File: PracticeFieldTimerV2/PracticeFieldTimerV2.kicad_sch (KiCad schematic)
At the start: 17 parts, among them J1 External Controls, J3 Panel, J5 /CAN Enable, J6 RJ45, J7 RJ45, U1 ESP32-DevKitC

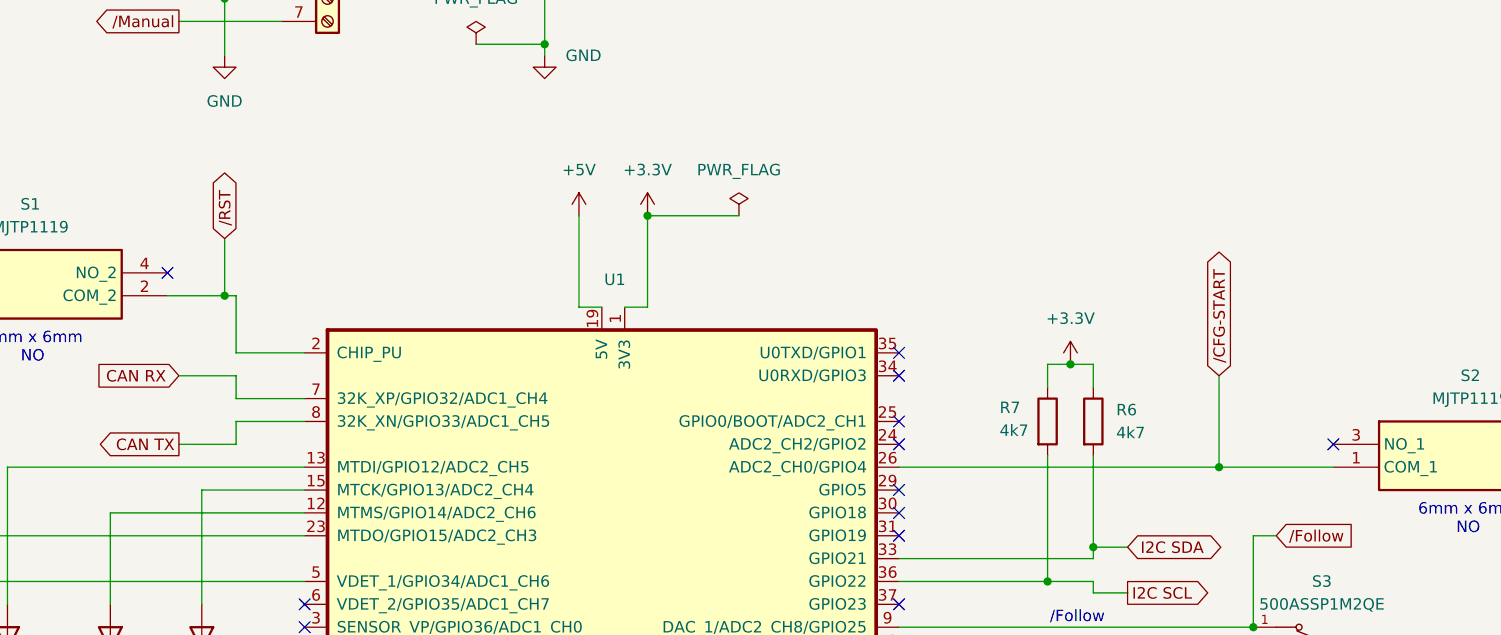
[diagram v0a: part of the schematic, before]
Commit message: Fix push button connections.
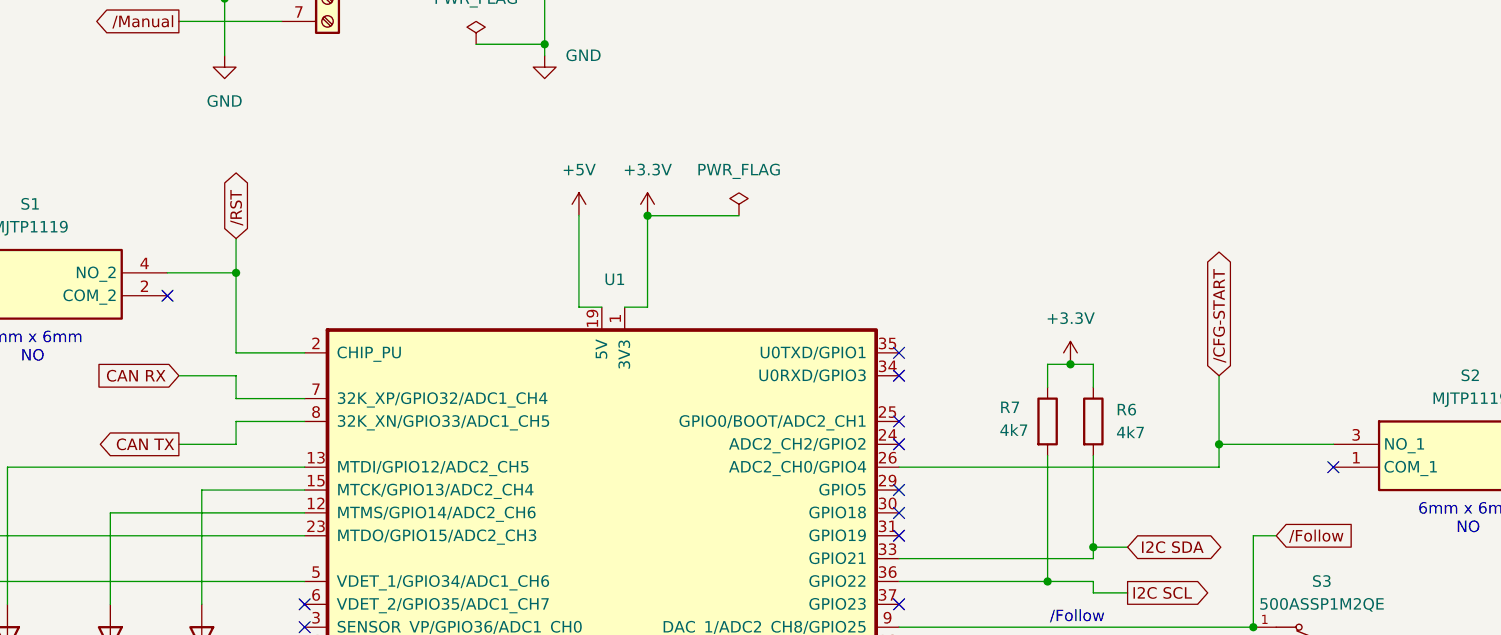
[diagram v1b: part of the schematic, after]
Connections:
- net /CFG-START: now also S2.3 (NO_1); no longer S2.1 (COM_1)
- net /RST: now also S1.4 (NO_2); no longer S1.2 (COM_2)
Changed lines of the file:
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@@
+	)
+	(junction
+		(at 204.47 85.09)
+		(diameter 0)
+		(color 0 0 0 0)
 	)
 	(junction
@@
 	)
 	(junction
-		(at 204.47 87.63)
-		(diameter 0)
-		(color 0 0 0 0)
-	)
-	(junction
 		(at 93.98 30.48)
 		(diameter 0)
@@
 	)
 	(junction
-		(at 93.98 68.58)
+		(at 95.25 66.04)
 		(diameter 0)
 		(color 0 0 0 0)
@@
 	)
 	(no_connect
-		(at 217.17 85.09)
+		(at 217.17 87.63)
 	)
 	(no_connect
@@
 	)
 	(no_connect
-		(at 87.63 66.04)
+		(at 87.63 68.58)
 	)
 	(no_connect
@@
 	(wire
 		(pts
+			(xy 204.47 85.09) (xy 204.47 87.63)
+		)
+		(stroke
+			(width 0)
+			(type default)
+		)
+	)
+	(wire
+		(pts
 			(xy 208.28 120.65) (xy 208.28 110.49)
 		)
@@
 	(wire
 		(pts
+			(xy 204.47 85.09) (xy 217.17 85.09)
+		)
+		(stroke
+			(width 0)
+			(type default)
+		)
+	)
+	(wire
+		(pts
 			(xy 121.92 40.64) (xy 129.54 40.64)
 		)
@@
 	(wire
 		(pts
-			(xy 204.47 87.63) (xy 217.17 87.63)
-		)
-		(stroke
-			(width 0)
-			(type default)
-		)
-	)
-	(wire
-		(pts
-			(xy 95.25 68.58) (xy 95.25 74.93)
-		)
-		(stroke
-			(width 0)
-			(type default)
-		)
-	)
-	(wire
-		(pts
 			(xy 135.89 179.07) (xy 135.89 181.61)
 		)
@@
 	(wire
 		(pts
+			(xy 87.63 66.04) (xy 95.25 66.04)
+		)
+		(stroke
+			(width 0)
+			(type default)
+		)
+	)
+	(wire
+		(pts
 			(xy 81.28 110.49) (xy 81.28 114.3)
 		)
@@
 	(wire
 		(pts
-			(xy 93.98 68.58) (xy 95.25 68.58)
+			(xy 95.25 66.04) (xy 95.25 74.93)
 		)
 		(stroke
@@
 	(wire
 		(pts
-			(xy 93.98 62.23) (xy 93.98 68.58)
+			(xy 95.25 62.23) (xy 95.25 66.04)
 		)
 		(stroke
@@
 	(wire
 		(pts
-			(xy 204.47 77.47) (xy 204.47 87.63)
+			(xy 204.47 77.47) (xy 204.47 85.09)
 		)
 		(stroke
@@
 		(pts
 			(xy 88.9 38.1) (xy 100.33 38.1)
-		)
-		(stroke
-			(width 0)
-			(type default)
-		)
-	)
-	(wire
-		(pts
-			(xy 87.63 68.58) (xy 93.98 68.58)
 		)
 		(stroke
@@
 	(global_label "{slash}RST"
 		(shape bidirectional)
-		(at 93.98 62.23 90)
+		(at 95.25 62.23 90)
 		(fields_autoplaced yes)
 		(effects
@@
 		)
 		(property "Intersheetrefs" "${INTERSHEET_REFS}"
-			(at 93.98 53.3559 90)
+			(at 95.25 53.3559 90)
 			(effects
 				(font

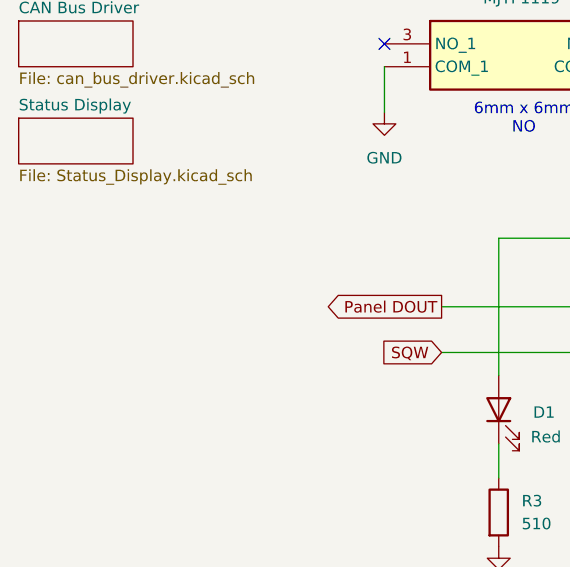
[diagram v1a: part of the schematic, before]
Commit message: Add DS3231
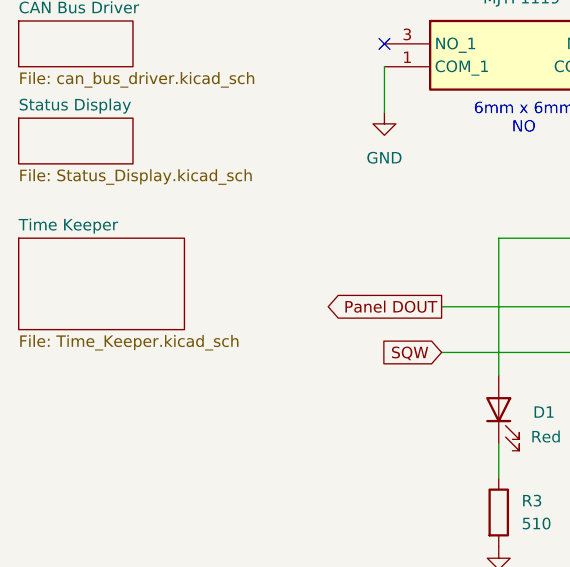
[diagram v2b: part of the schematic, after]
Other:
- added sheet Time Keeper (Time_Keeper.kicad_sch)
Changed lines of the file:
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@@
+	)
+	(sheet
+		(at 16.51 87.63)
+		(size 18.415 10.16)
+		(exclude_from_sim no)
+		(in_bom yes)
+		(on_board yes)
+		(dnp no)
+		(fields_autoplaced yes)
+		(stroke
+			(width 0.1524)
+			(type solid)
+		)
+		(fill
+			(color 0 0 0 0.0000)
+		)
+		(property "Sheetname" "Time Keeper"
+			(at 16.51 86.9184 0)
+			(effects
+				(font
+					(size 1.27 1.27)
+				)
+				(justify left bottom)
+			)
+		)
+		(property "Sheetfile" "Time_Keeper.kicad_sch"
+			(at 16.51 98.3746 0)
+			(effects
+				(font
+					(size 1.27 1.27)
+				)
+				(justify left top)
+			)
+		)
+		(instances
+			(project "PracticeFieldTimerV2"
+				(path "/a82ebad5-0442-461b-8944-6652da9a0796"
+					(page "4")
+				)
+			)
+		)
 	)
 	(sheet

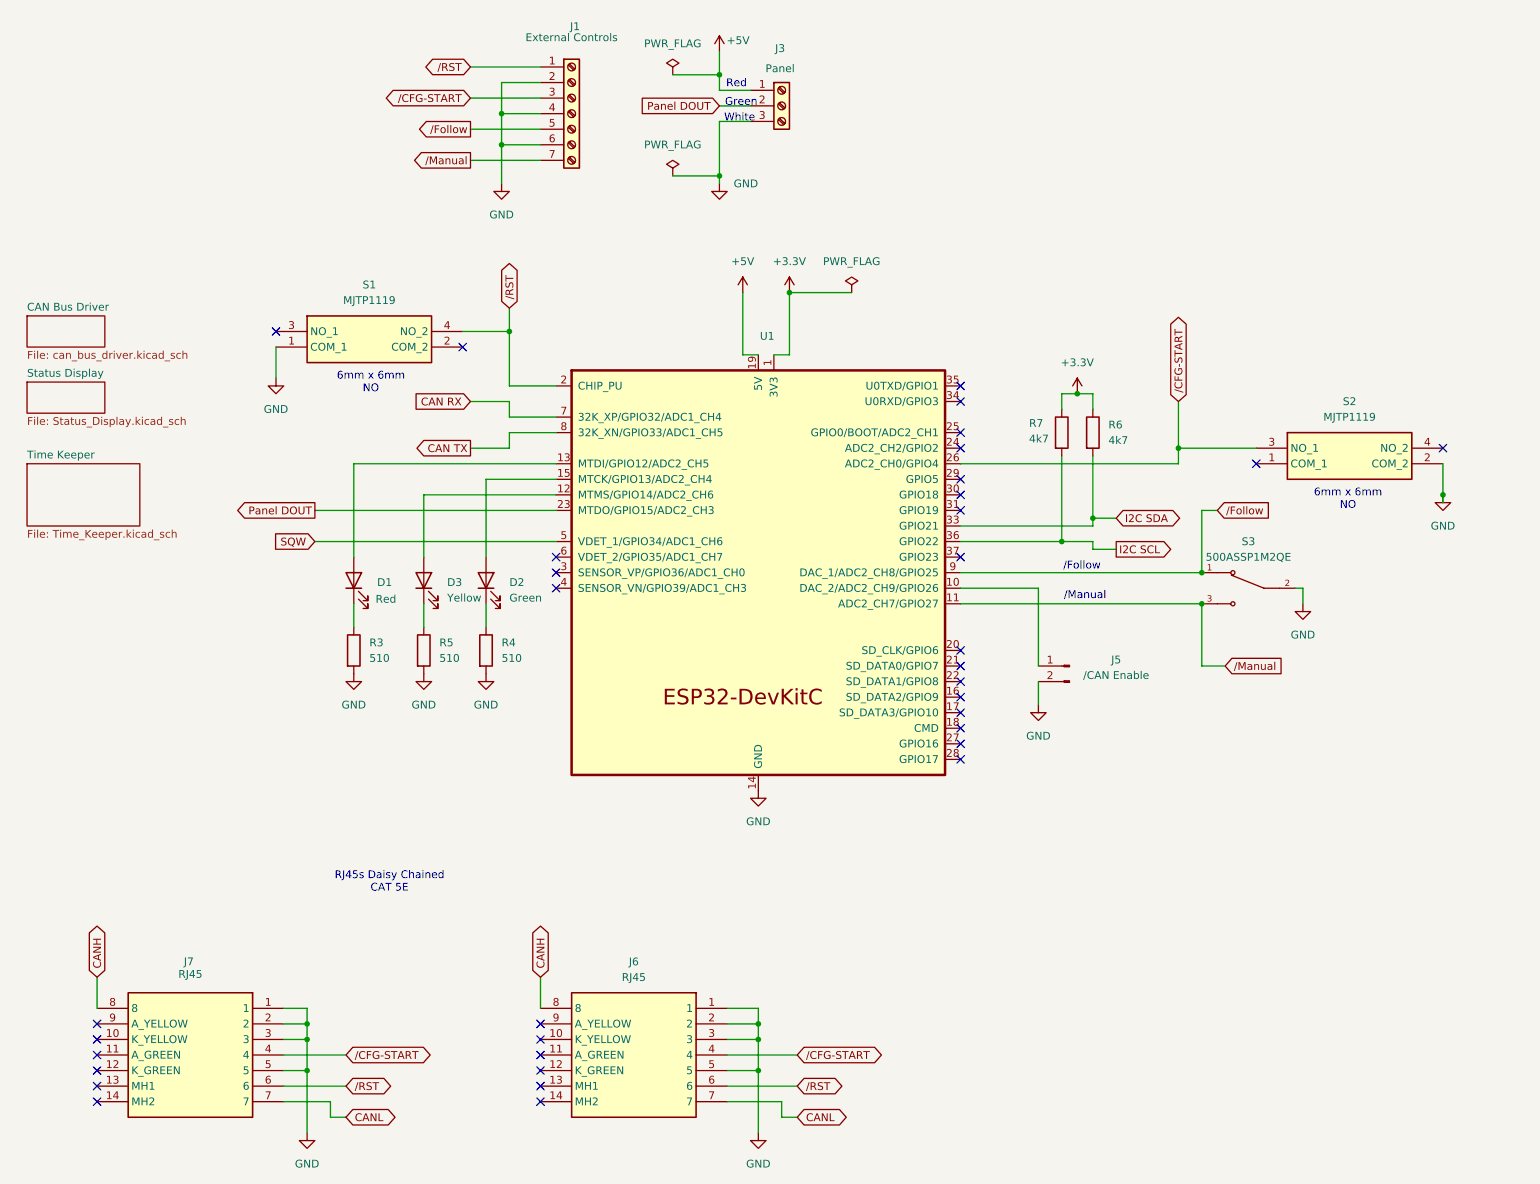
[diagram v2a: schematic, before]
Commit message: Morar blinkinlights: connect the LEDs on the RJ45 jacks to ESP32 pins. Can have too many blinkers!
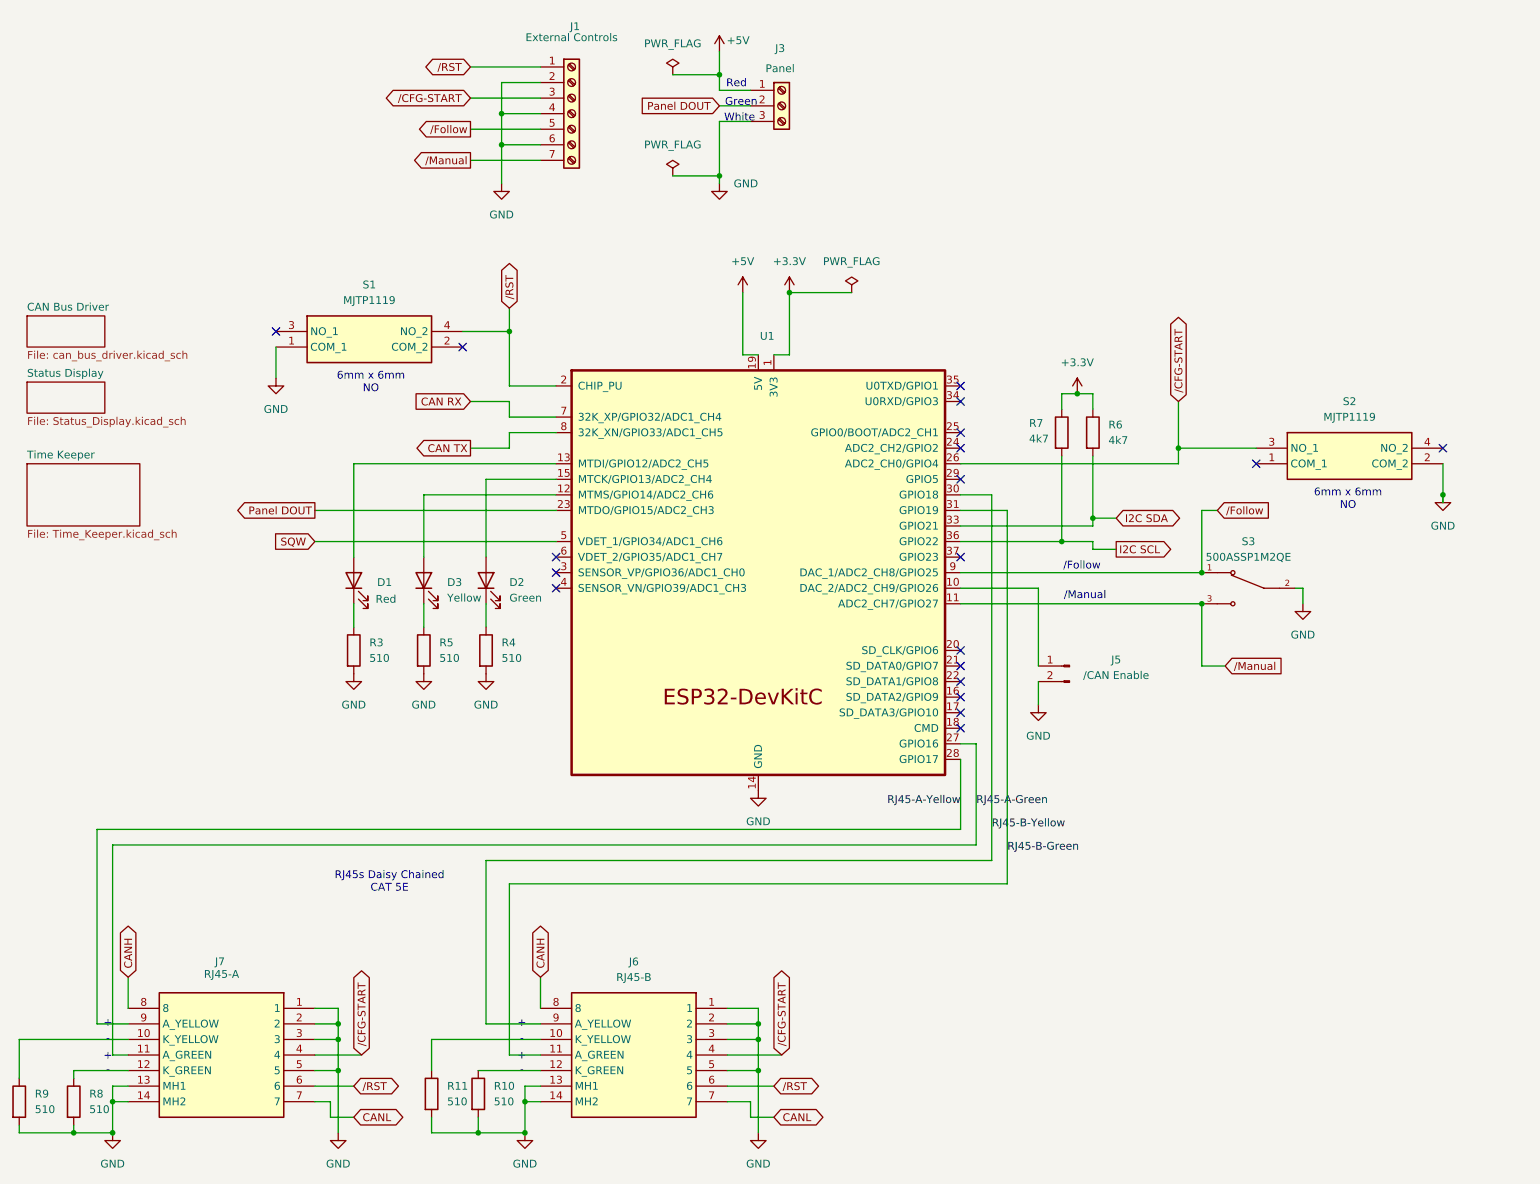
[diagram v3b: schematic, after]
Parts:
- added R10, R11, R8, R9: 510, Resistor_THT:R_Axial_DIN0207_L6.3mm_D2.5mm_P15.24mm_Horizontal, symbol Device:R
- J6: value RJ45 -> RJ45-B
- J7: value RJ45 -> RJ45-A
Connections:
- net GND: now also J6.13 (MH1), J6.14 (MH2), J7.13 (MH1), J7.14 (MH2), R10.2, R11.2, R8.2, R9.2
- net RJ45-A-Green: now reaches U1.27 (GPIO16)
- net RJ45-A-Green: now also J7.11 (A_GREEN)
- net RJ45-A-Yellow: now reaches U1.28 (GPIO17)
- net RJ45-A-Yellow: now also J7.9 (A_YELLOW)
- net RJ45-B-Yellow: now reaches U1.30 (GPIO18)
- net RJ45-B-Yellow: now also J6.9 (A_YELLOW)
- net RJ45-B-Green: now reaches U1.31 (GPIO19)
- net RJ45-B-Green: now also J6.11 (A_GREEN)
- net at J7.10 (K_YELLOW): now also R9.1
- net at J7.12 (K_GREEN): now also R8.1
- net at J6.10 (K_YELLOW): now also R11.1
- net at J6.12 (K_GREEN): now also R10.1
- no-connect marks 35 -> 19
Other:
- note added: "+"
- note added: "-"
- moved on the sheet: J7

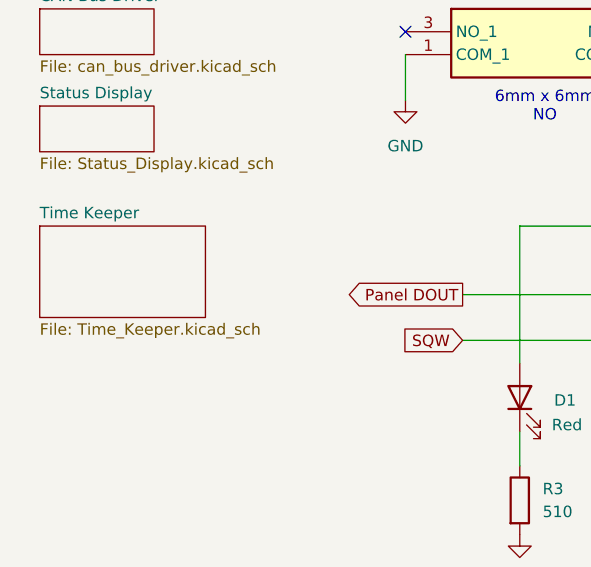
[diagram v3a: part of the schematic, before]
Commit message: More cleanup: redraw the cut lines to precise dimensions, minor improvements to symbol appearance.
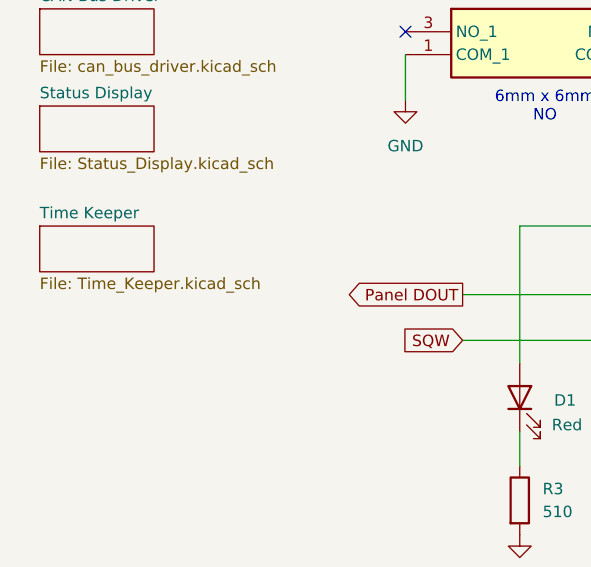
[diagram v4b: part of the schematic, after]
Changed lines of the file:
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@@
 	(sheet
 		(at 16.51 87.63)
-		(size 18.415 10.16)
+		(size 12.7 5.08)
 		(exclude_from_sim no)
 		(in_bom yes)
@@
 		)
 		(property "Sheetfile" "Time_Keeper.kicad_sch"
-			(at 16.51 98.3746 0)
+			(at 16.51 93.2946 0)
 			(effects
 				(font

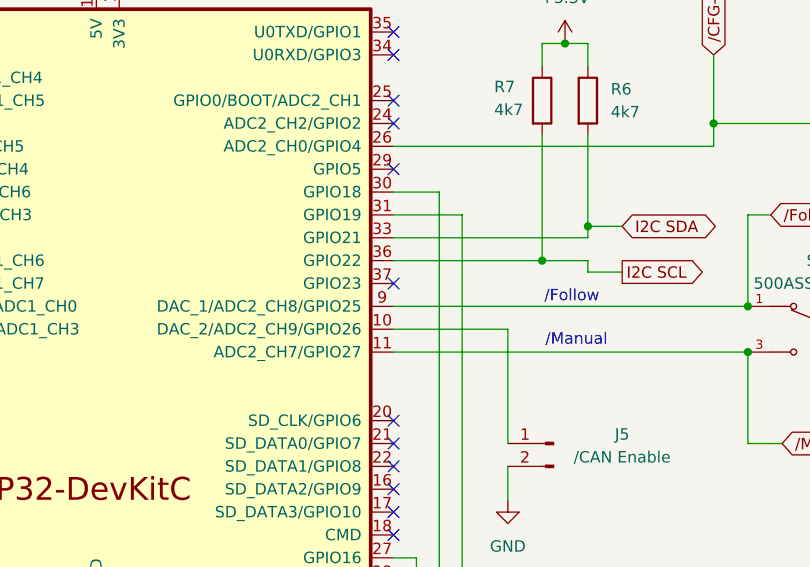
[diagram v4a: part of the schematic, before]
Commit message: Fix egregious wiring error in the LCD Display
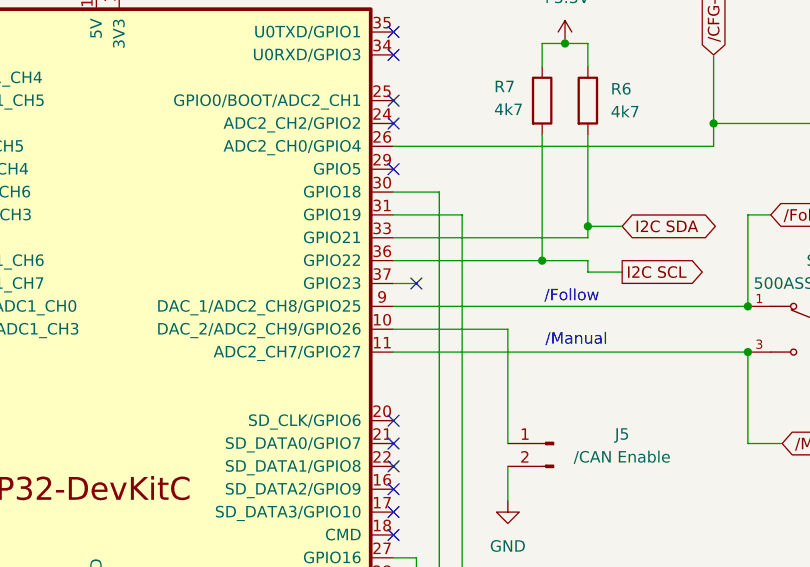
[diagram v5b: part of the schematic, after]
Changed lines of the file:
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@@
 	)
 	(no_connect
-		(at 168.91 102.87)
+		(at 171.45 102.87)
 	)
 	(no_connect
@@
 		)
 		(stroke
+			(width 0)
+			(type default)
+		)
+	)
+	(wire
+		(pts
+			(xy 171.45 102.87) (xy 168.91 102.87)
+		)
+		(stroke

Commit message: Fix reversed power and ground on LCD backlight LED.
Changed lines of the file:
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@@
 	)
 	(sheet
-		(at 16.51 87.63)
-		(size 12.7 5.08)
+		(at 16.51 86.36)
+		(size 12.7 5.715)
 		(exclude_from_sim no)
 		(in_bom yes)
@@
 		)
 		(property "Sheetname" "Time Keeper"
-			(at 16.51 86.9184 0)
+			(at 16.51 85.6484 0)
 			(effects
 				(font
@@
 		)
 		(property "Sheetfile" "Time_Keeper.kicad_sch"
-			(at 16.51 93.2946 0)
+			(at 16.51 92.6596 0)
 			(effects
 				(font
